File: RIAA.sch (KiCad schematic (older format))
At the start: 37 parts, among them J13 Conn_01x03_Female, J23 Conn_01x03_Female, SW101 SW_DPDT_x2, U1 NE5532

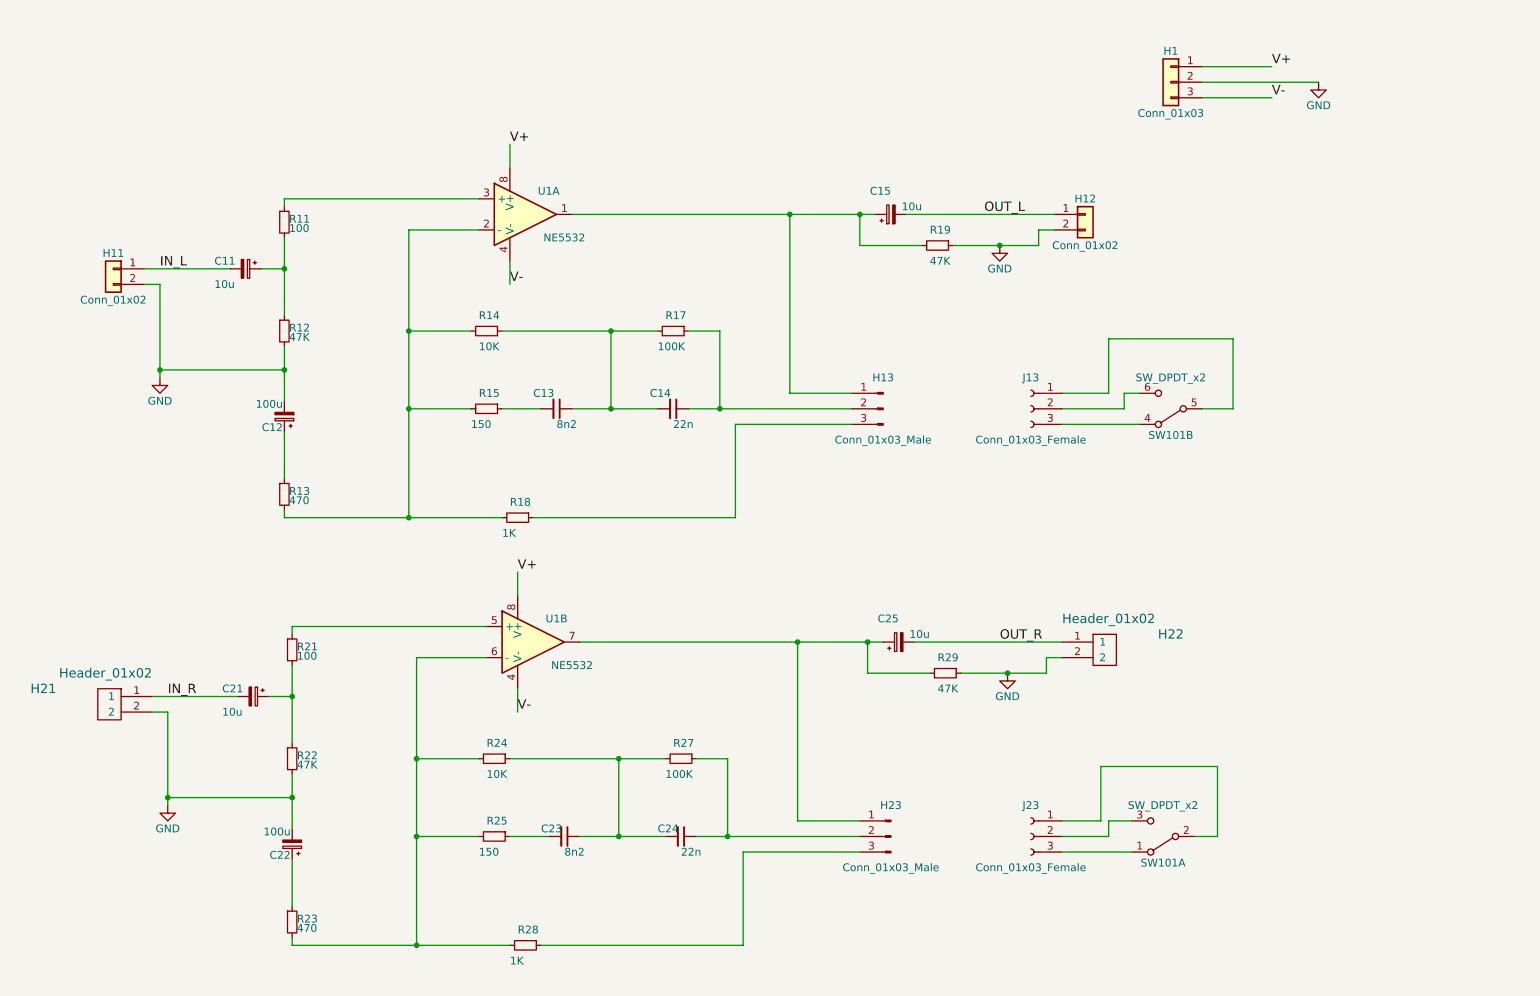
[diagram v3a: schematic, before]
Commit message: Updating components references
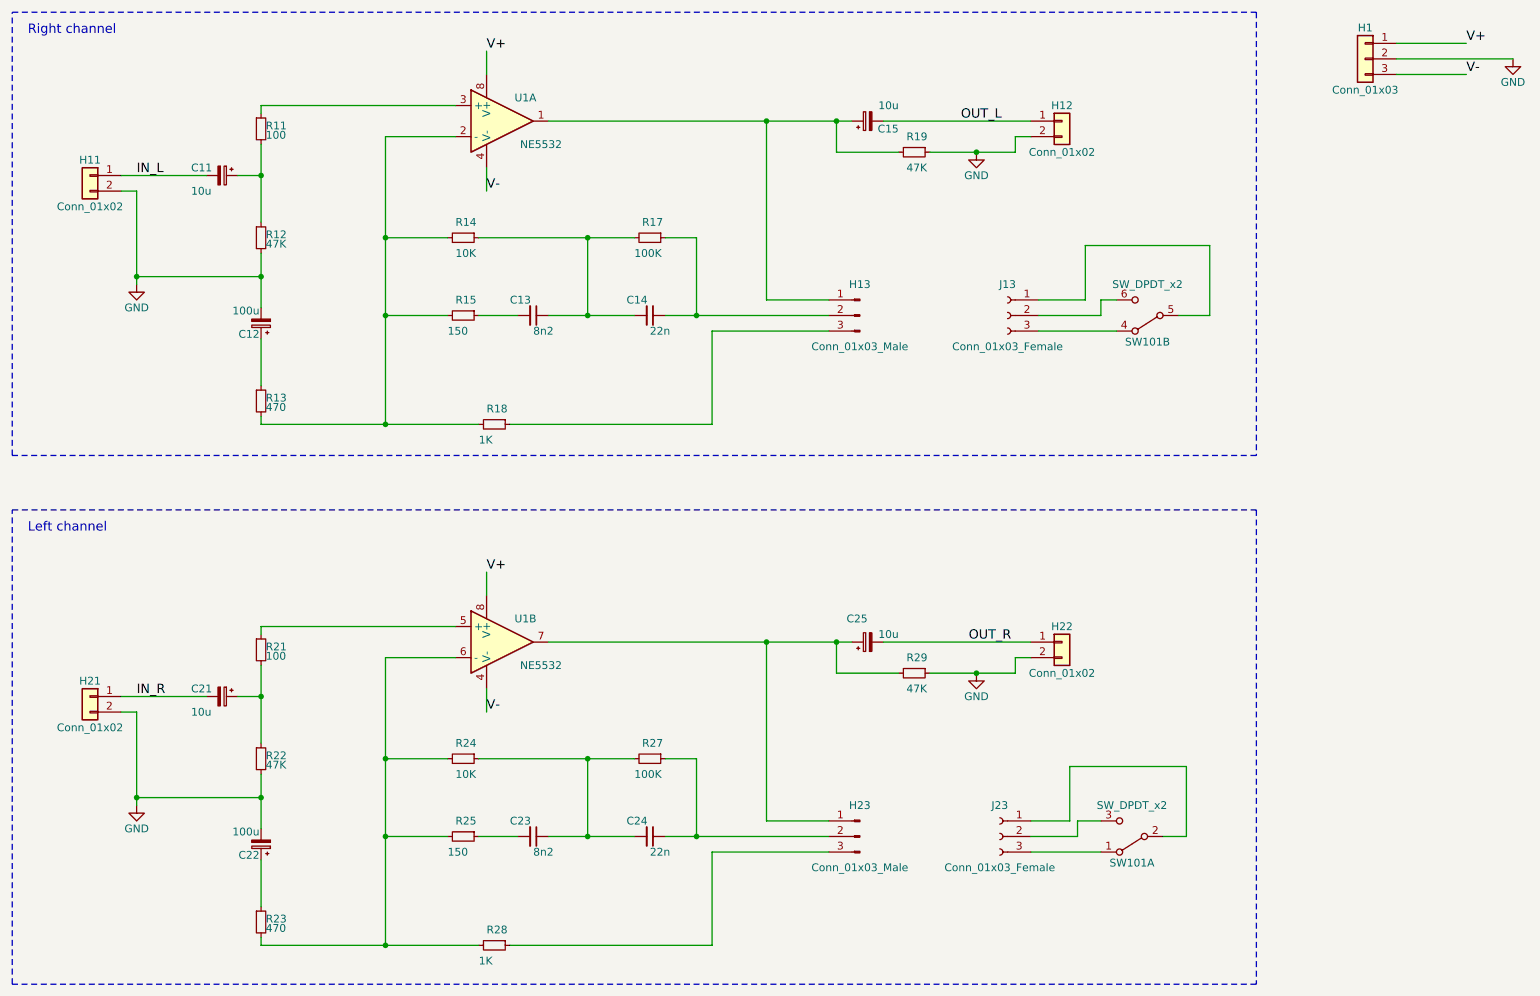
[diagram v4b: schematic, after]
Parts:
- removed H21, H22: Header_01x02, Pin_Headers:Pin_Header_Straight_1x02, symbol Header_01x02
- added H21, H22: Conn_01x02, symbol Conn_01x02
- C11, C21: Description (none) -> Aluminium Electrolytic Capacitors - Leaded 35volts 10uF; Distributor (none) -> Mouser; Distributor Part # (none) -> 647-UVR1V100MDD1TA; Manufacturer (none) -> Nichicon; Package (none) -> 2-THT
- C12, C22: Description (none) -> Aluminium Electrolytic Capacitors - Leaded 10volts 100uF 5x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; Distributor (none) -> Mouser; Distributor Part # (none) -> 647-UVR1A101MDD; Manufacturer (none) -> Nichicon; Package (none) -> 2-THT
- C13, C23: footprint Capacitors_ThroughHole:C_Rect_L7_W2.5_P5 -> Capacitors_ThroughHole:C_Rect_L7.2mm_W2.5mm_P5.00mm_FKS2_FKP2_MKS2_MKP2; Description (none) -> Film Capacitors 50volts 8200pF 5% LS 5mm; Distributor (none) -> Mouser; Distributor Part # (none) -> 80-MMK5822J50J01L4; Manufacturer (none) -> KEMET; Mfg_Part_No QYX2A822KTP -> MMK5822J50J01L4BULK; Package (none) -> 2-THT
- C14, C24: footprint Capacitors_ThroughHole:C_Rect_L7_W2.5_P5 -> Capacitors_ThroughHole:C_Rect_L7.2mm_W2.5mm_P5.00mm_FKS2_FKP2_MKS2_MKP2; Description (none) -> Film Capacitors 100volts 0.022uF 5%; Distributor (none) -> Mouser; Distributor Part # (none) -> 80-R82EC2220AA50J; Manufacturer (none) -> KEMET; Mfg_Part_No QYX2A223KTP -> R82EC2220AA50J; Package (none) -> 2-THT
- C15: Description (none) -> Aluminium Electrolytic Capacitors - Leaded 35volts 10uF; Distributor (none) -> Mouser; Distributor Part # (none) -> 647-UVR1V100MDD1TA; Manufacturer (none) -> Nichicon; Mfg_Part_No UVR1A101MDD -> UVR1V100MDD1TA; Package (none) -> 2-THT
- H1: footprint (none) -> Pin_Headers:Pin_Header_Straight_1x03_Pitch2.54mm; Description (none) -> Headers & Wire Housings WR-PHD 2.54mm Hdr 3P Single Str Gold; Distributor (none) -> Mouser; Distributor Part # (none) -> 710-61300311121; Manufacturer (none) -> Wurth Electronics; Mfg_Part_No (none) -> 61300311121; Package (none) -> 3-THT
- H11: Distributor Part # (none) -> 710-61300211121; Manufacturer (none) -> Wurth Electronics; Mfg_Part_No (none) -> 61300211121
- H12: Description (none) -> Embases et logements de câbles WR-PHD 2.54mm Hdr 2P Single 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; Distributor (none) -> Mouser; Distributor Part # (none) -> 710-61300211121; Manufacturer (none) -> Wurth Electronics; Mfg_Part_No (none) -> 61300211121; Package (none) -> 2-THT
- H13, H23: Mfg_Part_No (none) -> 22-27-2031
- J13, J23: Mfg_Part_No (none) -> 22-01-3037
- R11, R21: footprint Resistors_ThroughHole:Resistor_Horizontal_RM10mm -> Resistors_ThroughHole:R_Axial_DIN0204_L3.6mm_D1.6mm_P5.08mm_Horizontal; Description (none) -> Metal Film Resistors - Through Hole 1/3watts 100ohms 1%; Distributor (none) -> Mouser; Distributor Part # (none) -> 71-CCF50-100; Manufacturer (none) -> Vishay / Dale; Mfg_Part_No CCF07100RJKE36 -> CCF50100RFKR36; Package (none) -> DIN0204
- R12, R22: footprint Resistors_ThroughHole:Resistor_Horizontal_RM10mm -> Resistors_ThroughHole:R_Axial_DIN0204_L3.6mm_D1.6mm_P5.08mm_Horizontal; Description (none) -> Metal Film Resistors - Through Hole 1/2watt 47Kohms 5%; Distributor (none) -> Mouser; Distributor Part # (none) -> 594-SFR16S0004702JA5; Manufacturer (none) -> Vichay / BC Components; Mfg_Part_No CCF0747K0GKE36 -> SFR16S0004702JA500; Package (none) -> 2-THT
- R13, R23: footprint Resistors_ThroughHole:Resistor_Horizontal_RM10mm -> Resistors_ThroughHole:R_Axial_DIN0204_L3.6mm_D1.6mm_P5.08mm_Horizontal; Description (none) -> Metal Film Resistors - Through Hole 1/2watt 470ohms 5%; Distributor (none) -> Mouser; Distributor Part # (none) -> 594-SFR16S0004700JA5; Manufacturer (none) -> Vishay / BC Components; Mfg_Part_No CCF07470RGKE36 CCF07470RGKE36 CCF07470RGKE36 -> SFR16S0004700JA500; Package (none) -> 2-THT
- R14, R24: footprint Resistors_ThroughHole:Resistor_Horizontal_RM10mm -> Resistors_ThroughHole:R_Axial_DIN0204_L3.6mm_D1.6mm_P5.08mm_Horizontal; Description (none) -> Metal Film Resistors - Through Hole 1/3watts 10Kohms 1%; Distributor (none) -> Mouser; Distributor Part # (none) -> 71-CCF5010K0FKE36; Manufacturer (none) -> Vishay / Dale; Mfg_Part_No CCF0710K0GKE36 -> CCF5010K0FKE36; Package (none) -> DIN0204
- R15, R25: footprint Resistors_ThroughHole:Resistor_Horizontal_RM10mm -> Resistors_ThroughHole:R_Axial_DIN0204_L3.6mm_D1.6mm_P5.08mm_Horizontal; Description (none) -> Metal Film Resistors - Through Hole 1/3watts 150ohms 1%; Distributor (none) -> Mouser; Distributor Part # (none) -> 71-CCF50-150; Manufacturer (none) -> Vishay / Dale; Mfg_Part_No CCF07150RGKE36 -> CCF50150RFKR36; Package (none) -> 2-THT
- R17, R27: footprint Resistors_ThroughHole:Resistor_Horizontal_RM10mm -> Resistors_ThroughHole:R_Axial_DIN0204_L3.6mm_D1.6mm_P5.08mm_Horizontal; Description (none) -> Metal Film Resistors - Through Hole 1/4watt 100Kohms 1%; Distributor (none) -> Mouser; Distributor Part # (none) -> 71-CMF50100K00FHEB; Manufacturer (none) -> Vishay / Dale; Mfg_Part_No CCF07100KGKE36 -> CMF50100K00FHEB; Package (none) -> DIN0204
- R18, R28: footprint Resistors_ThroughHole:Resistor_Horizontal_RM10mm -> Resistors_ThroughHole:R_Axial_DIN0204_L3.6mm_D1.6mm_P5.08mm_Horizontal; Description (none) -> Metal Film Resistors - Through Hole 1/3watts 1Kohms 1%; Distributor (none) -> Mouser; Distributor Part # (none) -> 71-CCF501K00FKE36; Manufacturer (none) -> Vishay / Dale; Mfg_Part_No (none) -> CCF501K00FKE36; Package (none) -> 2-THT
- R19, R29: footprint Resistors_ThroughHole:Resistor_Horizontal_RM10mm -> Resistors_ThroughHole:R_Axial_DIN0204_L3.6mm_D1.6mm_P5.08mm_Horizontal; Description (none) -> Metal Film Resistors - Through Hole 1/2watt 47Kohms 5%; Distributor (none) -> Mouser; Distributor Part # (none) -> 594-SFR16S0004702JA5; Manufacturer (none) -> Vishay / BC Components; Mfg_Part_No CCF0747K0GKE36 -> SFR16S0004702JA500; Package (none) -> 2-THT
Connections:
- net GND: now also H21.2 (Pin_2), H22.2 (Pin_2)
- net IN_R: now also H21.1 (Pin_1)
- net OUT_R: now also H22.1 (Pin_1)
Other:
- note added: "Left channel"
- note added: "Right channel"
- moved on the sheet: C11, C12, C13, C14, C25, H1, H11, H13, H23, J13, J23, R11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
